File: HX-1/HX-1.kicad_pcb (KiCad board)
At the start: 2 copper layers, 45 x 90 mm, 90 parts, among them J1 USB_C_Receptacle_USB2.0_16P, J10 Conn_01x24, J12 USART, J2 Conn_01x02_Socket, J3 I2C, J4 SPI, J8 UART, J9 Conn_01x24, SW1 BOOT0, U1 STM32H723ZGT6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

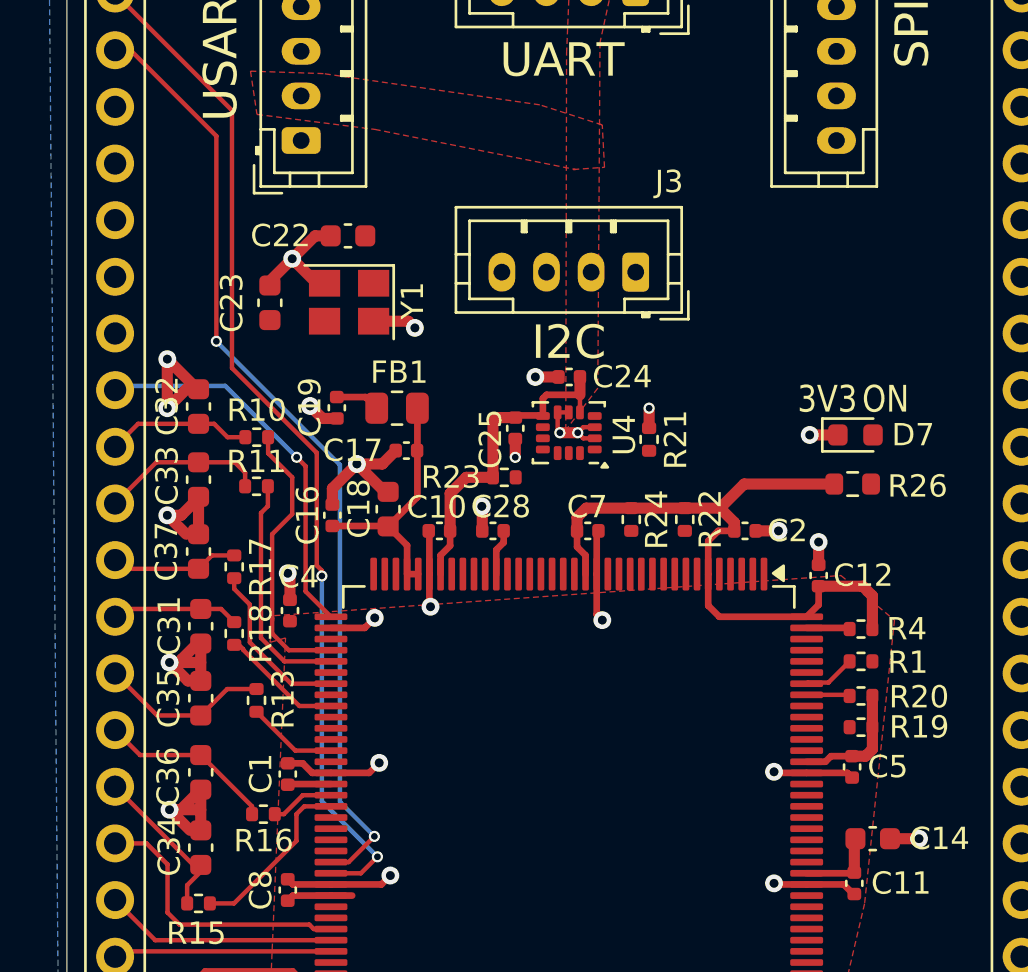
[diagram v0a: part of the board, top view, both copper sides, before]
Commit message: route USART traces, flip pin 18 and pin 19 on left header
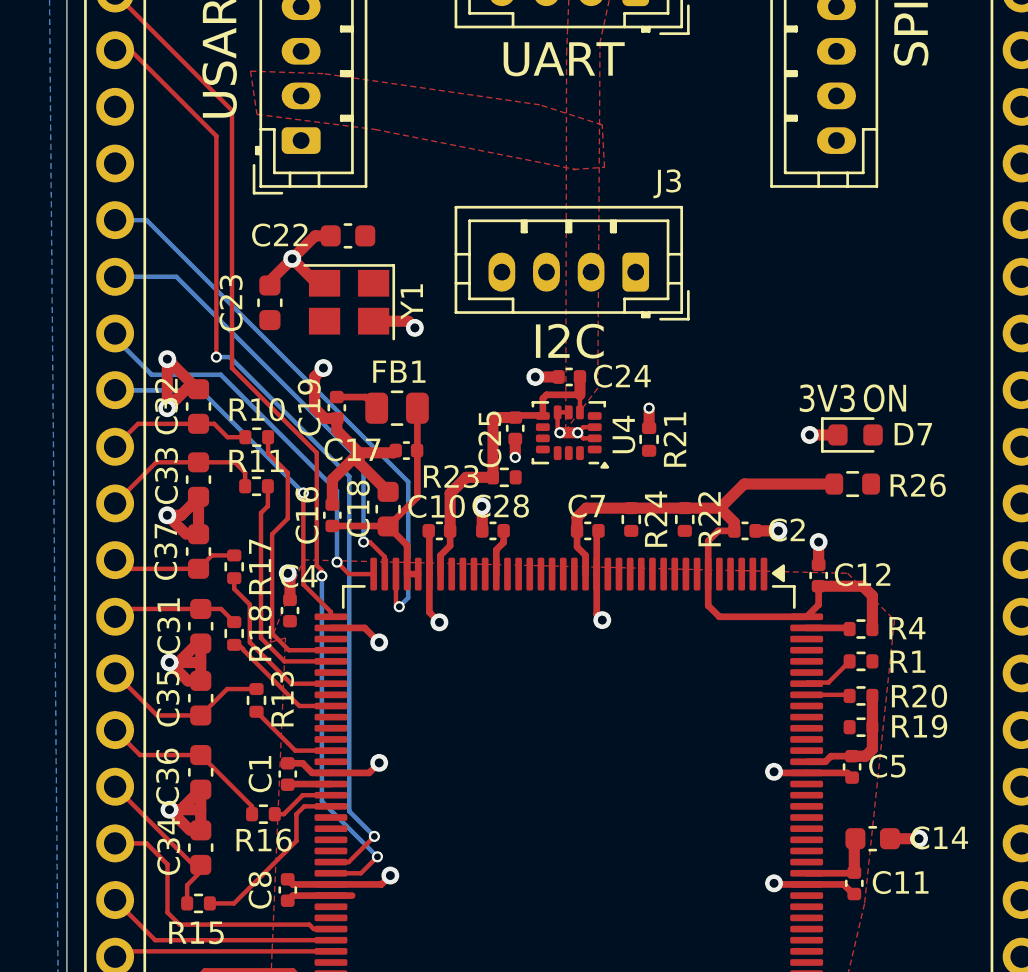
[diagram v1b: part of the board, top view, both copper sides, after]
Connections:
- J10 pad 18: /MCU/USART2_CTS -> /MCU/USART2_RTS
- J10 pad 19: /MCU/USART2_RTS -> /MCU/USART2_CTS
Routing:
- net /MCU/USART2_CTS: track 0.00 -> 26.0 mm, vias 0 -> 1
- net /MCU/USART2_RTS: track 0.00 -> 20.1 mm, vias 0 -> 1
- net /MCU/USART2_TX: track 0.00 -> 18.1 mm, vias 0 -> 1
- net GND: track 124.5 -> 130.0 mm, vias 42 -> 41
- net /MCU/USART2_RX: track 17.3 -> 16.4 mm

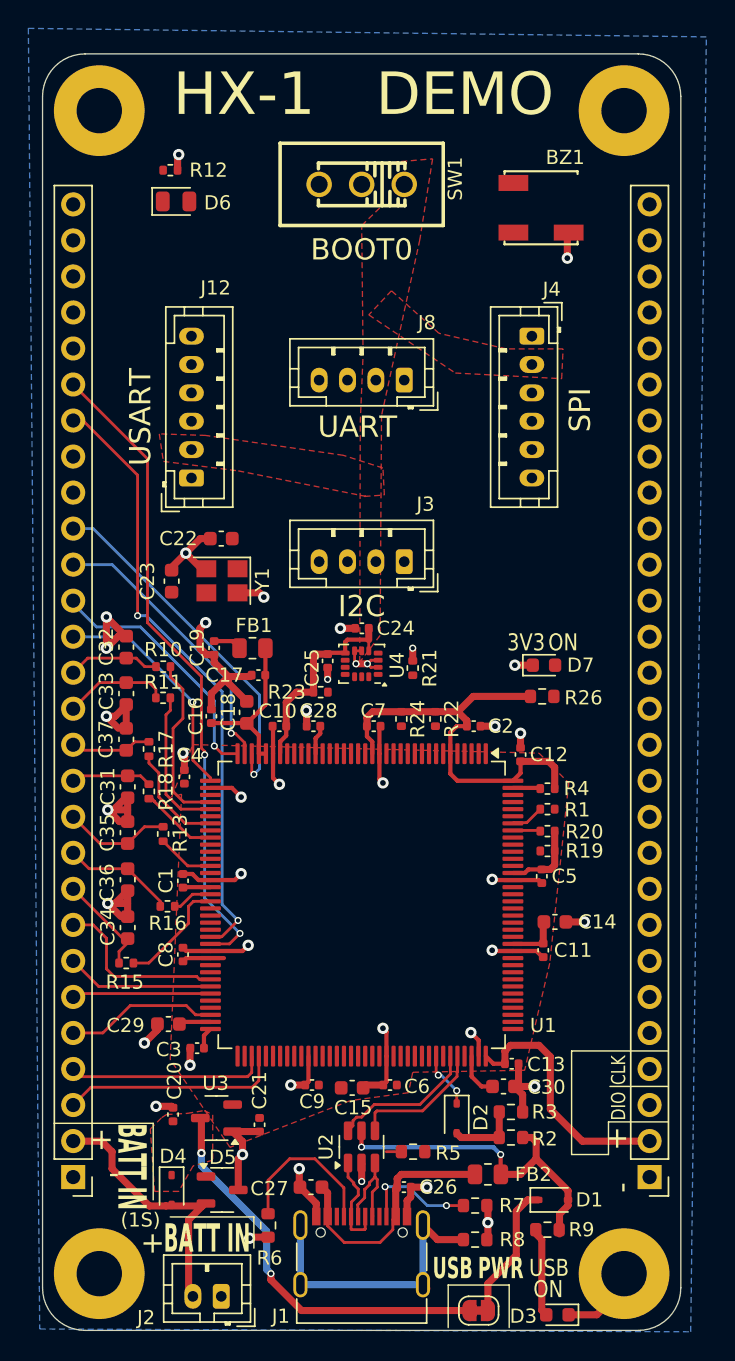
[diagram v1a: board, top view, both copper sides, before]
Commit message: route more of left side, change copper clearances based on jlcpcb
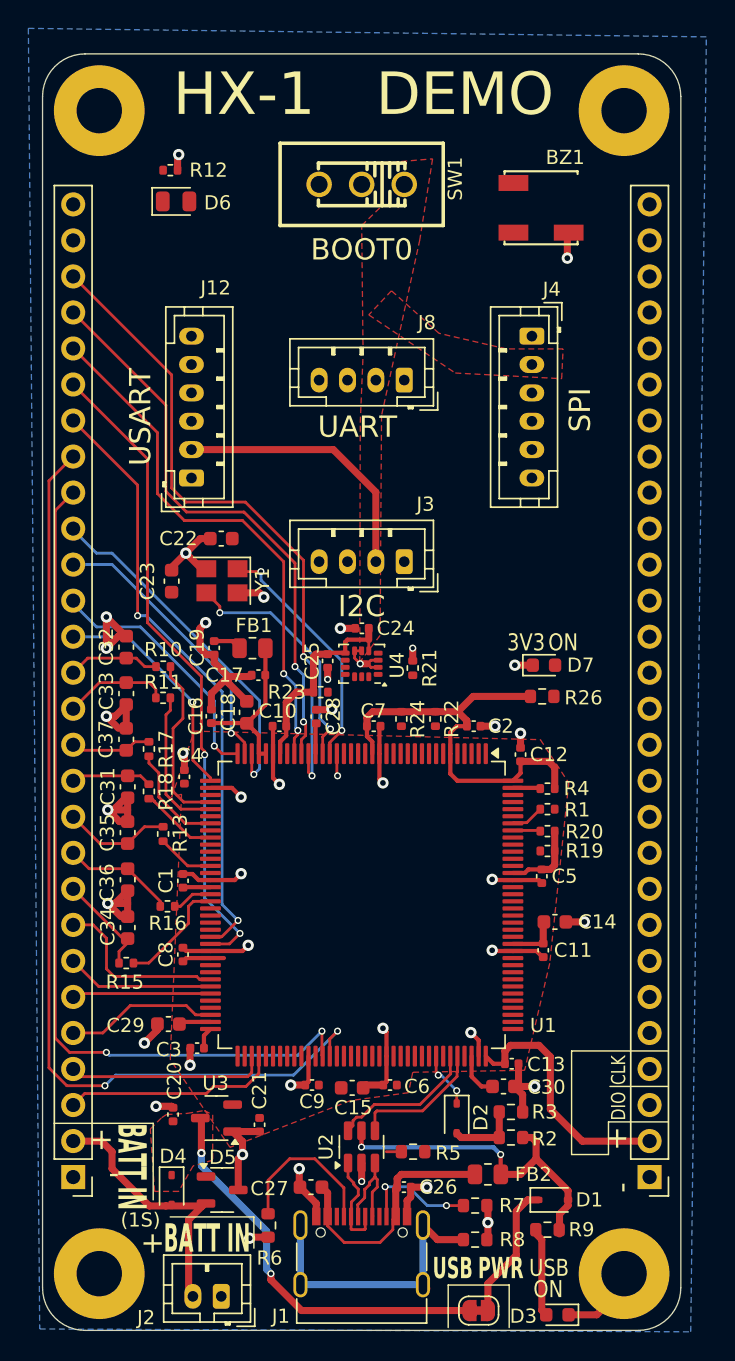
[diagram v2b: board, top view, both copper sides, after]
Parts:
- moved C28 0.71 mm to (146.3, 121.5), turned to 90 degrees
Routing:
- net /MCU/TIM4_PWM_4: track 0.00 -> 68.3 mm, vias 0 -> 2
- net /MCU/TIM4_PWM_3: track 0.00 -> 60.8 mm, vias 0 -> 2
- net /MCU/GPIO_9: track 0.00 -> 46.3 mm, vias 0 -> 2
- net /MCU/GPIO_10: track 0.00 -> 40.4 mm, vias 0 -> 2
- net /MCU/GPIO_11: track 0.00 -> 37.6 mm, vias 0 -> 2
- net +3.3V: track 81.4 -> 100.6 mm
- net RCC_OSC_OUT: track 0.00 -> 17.3 mm, vias 0 -> 2
- net RCC_OSC_IN: track 0.00 -> 17.3 mm, vias 0 -> 2
- net /MCU/GPIO_8: track 0.00 -> 1.58 mm, vias 0 -> 1
- net GND: track 130.0 -> 129.8 mm, vias 41 -> 40

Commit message: fix hole clearances, write custom rule for USB C to stop mechanical hole clearance error
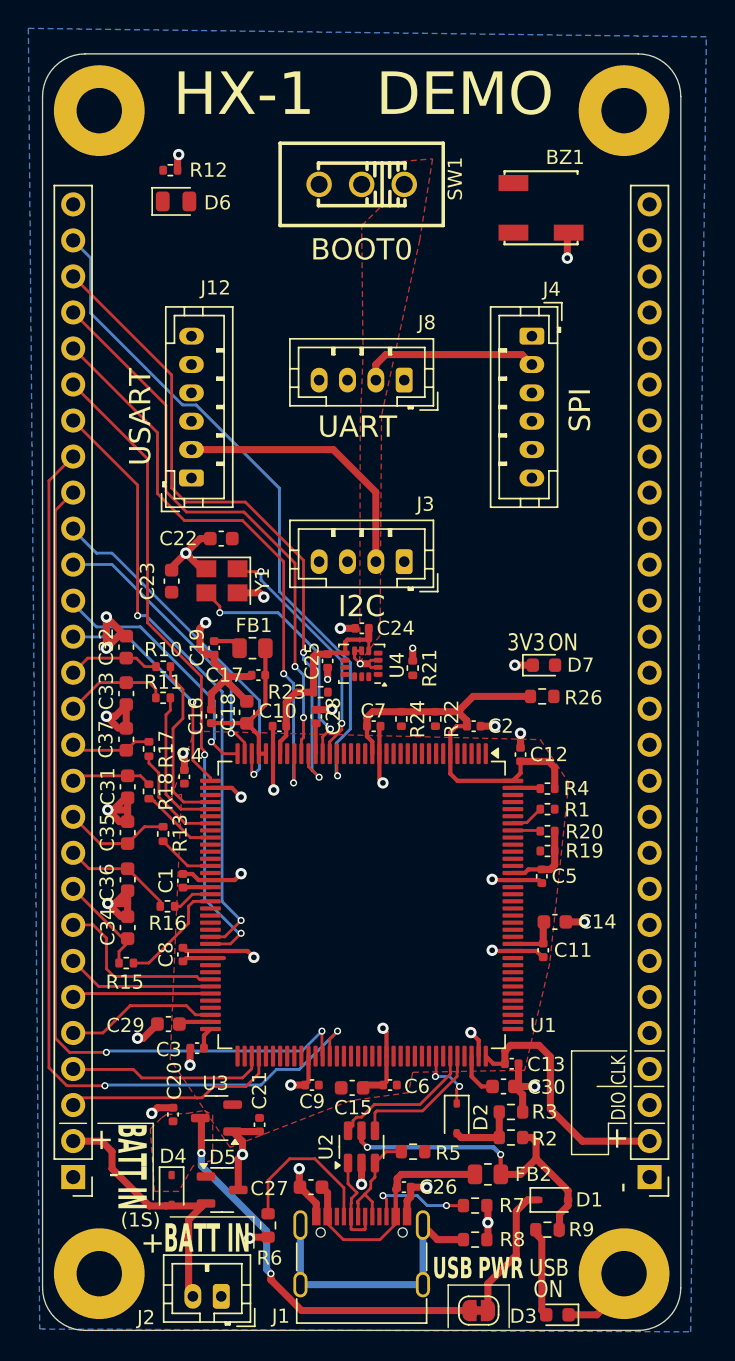
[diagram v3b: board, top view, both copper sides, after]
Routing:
- net /MCU/GPIO_8: track 1.58 -> 48.4 mm
- net +3.3V: track 100.6 -> 113.2 mm
- net /MCU/GPIO_11: track 37.6 -> 41.6 mm
- net GND: track 129.8 -> 131.2 mm
- net /Communication and Debug/CC2: track 8.22 -> 7.54 mm
- net USB_VBUS_SENSE: track 4.06 -> 4.73 mm
- net /MCU/GPIO_9: track 46.3 -> 46.9 mm

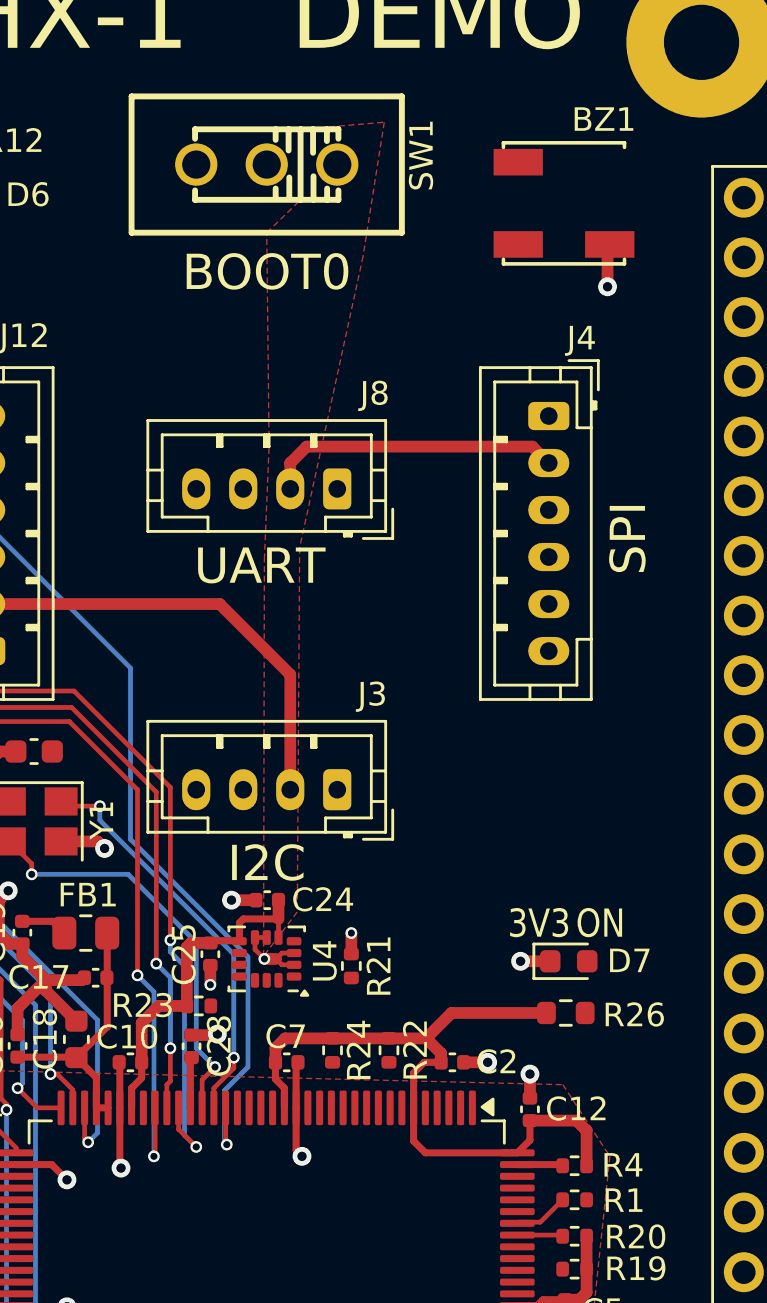
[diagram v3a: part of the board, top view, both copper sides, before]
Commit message: remove silkscreen too close to pad on buzzer, adjust via for gnd plane
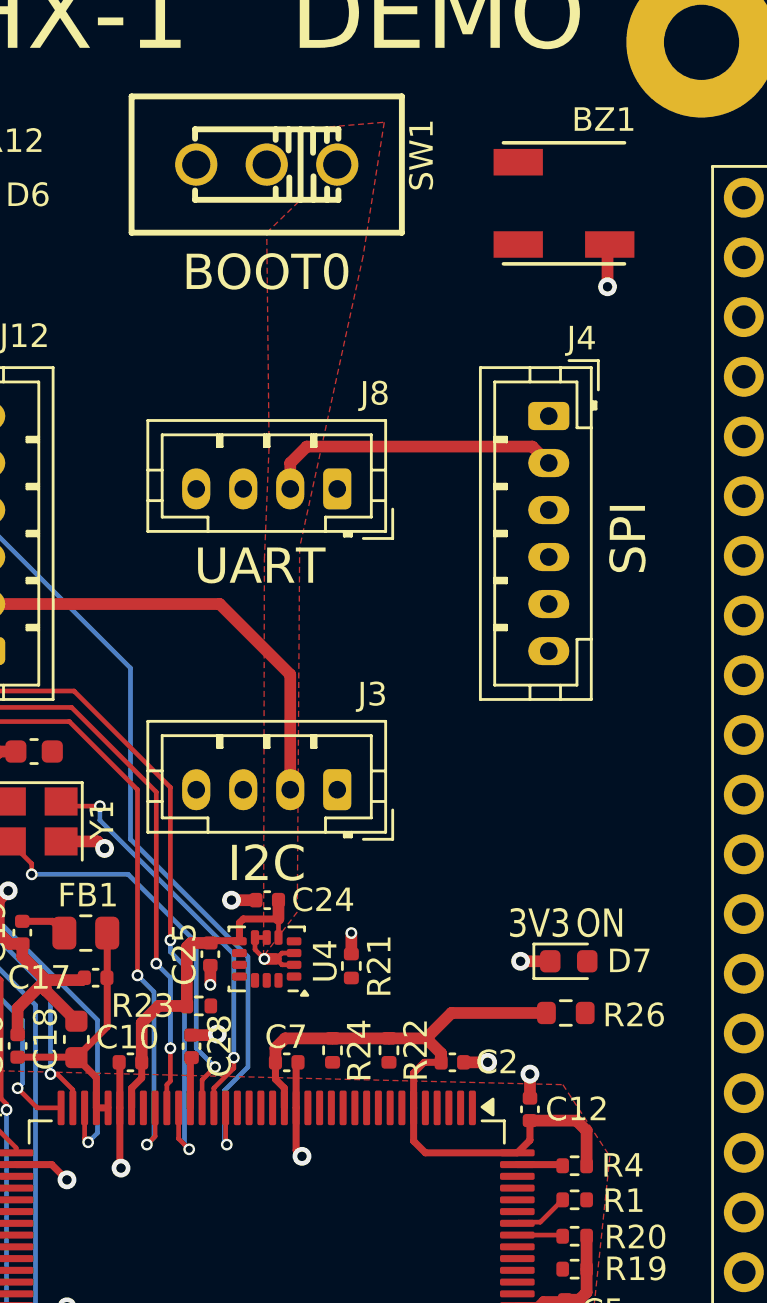
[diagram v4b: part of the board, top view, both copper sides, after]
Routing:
- net /MCU/GPIO_11: track 41.6 -> 40.8 mm
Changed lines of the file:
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@@
 		)
 		(fp_line
-			(start -2.376 3.619)
-			(end -2.376 3.424)
-			(stroke
-				(width 0.152)
-				(type solid)
-			)
-			(layer "F.SilkS")
-		)
-		(fp_line
-			(start -2.376 8.38)
-			(end -2.376 8.576)
-			(stroke
-				(width 0.152)
-				(type solid)
-			)
-			(layer "F.SilkS")
-		)
-		(fp_line
 			(start -2.376 8.576)
 			(end 2.776 8.576)
@@
 			(layer "F.SilkS")
 		)
-		(fp_line
-			(start 2.776 3.424)
-			(end 2.776 3.619)
-			(stroke
-				(width 0.152)
-				(type solid)
-			)
-			(layer "F.SilkS")
-		)
-		(fp_line
-			(start 2.776 8.576)
-			(end 2.776 8.38)
-			(stroke
-				(width 0.152)
-				(type solid)
-			)
-			(layer "F.SilkS")
-		)
 		(fp_poly
 			(pts
@@
 	)
 	(segment
-		(start 146.5 125.8)
-		(end 145.75 125.05)
-		(width 0.2)
-		(layer "F.Cu")
-		(net 137)
-	)
-	(segment
 		(start 141.3 106.4)
 		(end 137.1 106.4)
@@
 	)
 	(segment
-		(start 145.75 125.05)
+		(start 145.75 125.45)
 		(end 145.75 124.1375)
 		(width 0.2)
@@
 	)
 	(segment
+		(start 146.2 125.9)
+		(end 145.75 125.45)
+		(width 0.2)
+		(layer "F.Cu")
+		(net 137)
+	)
+	(segment
 		(start 136.1 105.4)
 		(end 136.1 97.43)
@@
 	)
 	(via
-		(at 146.5 125.8)
+		(at 146.2 125.9)
 		(size 0.5)
 		(drill 0.3)
@@
 	(segment
 		(start 145.4 117.5)
-		(end 146 118.1)
+		(end 145.4 117)
 		(width 0.2)
 		(layer "B.Cu")
@@
 	)
 	(segment
-		(start 146 125.3)
-		(end 146.5 125.8)
+		(start 146 125.7)
+		(end 146 118.1)
 		(width 0.2)
 		(layer "B.Cu")
@@
 	)
 	(segment
-		(start 145.4 117)
-		(end 145.4 117.5)
+		(start 146.2 125.9)
+		(end 146 125.7)
 		(width 0.2)
 		(layer "B.Cu")
@@
 	(segment
 		(start 146 118.1)
-		(end 146 125.3)
+		(end 145.4 117.5)
 		(width 0.2)
 		(layer "B.Cu")
@@
 	)
 	(segment
-		(start 141.1 107.7)
-		(end 137 107.7)
+		(start 144.4 125.7)
+		(end 144.75 125.35)
 		(width 0.2)
 		(layer "F.Cu")
@@
 	)
 	(segment
-		(start 144 110.6)
-		(end 141.1 107.7)
+		(start 141.1 107.7)
+		(end 137 107.7)
 		(width 0.2)
 		(layer "F.Cu")
@@
 	)
 	(segment
-		(start 144.75 126.15)
+		(start 144.75 125.35)
 		(end 144.75 124.1375)
 		(width 0.2)
@@
 	)
 	(segment
-		(start 144 118.5)
-		(end 144 110.6)
+		(start 144 110.6)
+		(end 141.1 107.7)
 		(width 0.2)
 		(layer "F.Cu")
@@
 	)
 	(segment
-		(start 144.7 126.2)
-		(end 144.75 126.15)
+		(start 144 118.5)
+		(end 144 110.6)
 		(width 0.2)
 		(layer "F.Cu")
@@
 	)
 	(via
-		(at 144.7 126.2)
+		(at 144.4 125.7)
 		(size 0.5)
 		(drill 0.3)
@@
 	)
 	(segment
-		(start 144.7 126.2)
+		(start 144.4 125.7)
+		(end 144.7 125.4)
+		(width 0.2)
+		(layer "B.Cu")
+		(net 141)
+	)
+	(segment
+		(start 144.7 125.4)
 		(end 144.7 119.2)
 		(width 0.2)
